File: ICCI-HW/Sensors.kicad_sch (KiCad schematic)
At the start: 25 parts, among them U301 DS18B20, U302 AS7341, U303 BH1750FVI-TR, U304 TCS34725FN, U305 TSL2561, U306 PCA9306GM,125

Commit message: hw: updates
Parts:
- U305: footprint ICCI-LIB:TLS2561 -> ICCI-LIB:TSL2561
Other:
- note added: "DS report no pull-up, Need testing."
- note removed: "DS report no pull-up, need testing."
- company: tollsimy -> Simone Tollardo
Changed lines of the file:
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@@
   (title_block
     (title "Sensors")
-    (date "2022-05-04")
+    (date "2022-07-14")
     (rev "BETA")
-    (company "tollsimy")
+    (company "Simone Tollardo")
   )
   (junction (at 78.105 134.62) (diameter 0) (color 0 0 0 0)
@@
     (effects (font (size 1.27 1.27)) (justify left bottom))
   )
-  (text "DS report\nno pull-up, \nneed testing." (at 69.215 118.11 0)
+  (text "DS report\nno pull-up, \nNeed testing." (at 69.215 118.11 0)
     (effects (font (size 1.27 1.27)) (justify left bottom))
   )
@@
     (effects (font (size 1.27 1.27)) (justify left bottom))
   )
-  (text "SENSORS" (at 62.865 19.685 180)
+  (text "SENSORS" (at 62.865 20.955 180)
     (effects (font (size 3 3) (thickness 0.6) bold) (justify right bottom))
   )
@@
     (property "Reference" "U305" (id 0) (at 63.5 85.725 0))
     (property "Value" "TSL2561" (id 1) (at 52.705 83.185 0))
-    (property "Footprint" "ICCI-LIB:TLS2561" (id 2) (at 52.705 94.615 0)
-      (effects (font (size 1.27 1.27)) (justify left bottom) hide)
-    )
+    (property "Footprint" "ICCI-LIB:TSL2561" (id 2) (at 52.705 94.615 0)
+      (effects (font (size 1.27 1.27)) (justify left bottom) hide)
+    )

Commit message: start layout
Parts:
- U301: footprint Package_TO_SOT_THT:TO-92_Inline -> ICCI-LIB:DS18B20 Hor.
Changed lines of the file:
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@@
       (effects (font (size 1.27 1.27)) (justify right))
     )
-    (property "Footprint" "Package_TO_SOT_THT:TO-92_Inline" (id 2) (at 21.59 175.895 0)
+    (property "Footprint" "ICCI-LIB:DS18B20 Hor." (id 2) (at 21.59 175.895 0)
       (effects (font (size 1.27 1.27)) hide)
     )

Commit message: layout updates
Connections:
- net ADDR: now reaches R302.1, U303.2 (ADDR)
- net DVI: now reaches C311.1, R303.2, U303.5 (DVI)
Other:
- moved on the sheet: R302
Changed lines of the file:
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@@
     (stroke (width 0) (type default) (color 0 0 0 0))
   )
-  (wire (pts (xy 62.865 70.485) (xy 64.135 70.485))
+  (wire (pts (xy 62.865 70.485) (xy 68.58 70.485))
     (stroke (width 0) (type default) (color 0 0 0 0))
   )
@@
     (effects (font (size 1.27 1.27)) (justify left bottom))
   )
+  (label "DVI" (at 64.77 51.435 0)
+    (effects (font (size 1.27 1.27)) (justify left bottom))
+  )
   (label "SDA0" (at 63.5 37.465 0)
     (effects (font (size 1.27 1.27)) (justify left bottom))
@@
     (effects (font (size 1.27 1.27)) (justify left bottom))
   )
+  (label "ADDR" (at 63.5 70.485 0)
+    (effects (font (size 1.27 1.27)) (justify left bottom))
+  )
   (hierarchical_label "SDA0" (shape bidirectional) (at 137.795 77.47 0)
     (effects (font (size 1.27 1.27)) (justify left))
@@
     (pin "2")
   )
-  (symbol (lib_id "Device:R") (at 64.135 74.295 0) (unit 1)
-    (in_bom yes) (on_board yes)
-    (property "Reference" "R302" (id 0) (at 65.405 73.025 0)
-      (effects (font (size 1.27 1.27)) (justify left))
-    )
-    (property "Value" "1k" (id 1) (at 65.405 75.565 0)
-      (effects (font (size 1.27 1.27)) (justify left))
-    )
-    (property "Footprint" "Resistor_SMD:R_0603_1608Metric" (id 2) (at 62.357 74.295 90)
-      (effects (font (size 1.27 1.27)) hide)
-    )
-    (property "Datasheet" "~" (id 3) (at 64.135 74.295 0)
+  (symbol (lib_id "Device:R") (at 68.58 74.295 0) (unit 1)
+    (in_bom yes) (on_board yes)
+    (property "Reference" "R302" (id 0) (at 69.85 73.025 0)
+      (effects (font (size 1.27 1.27)) (justify left))
+    )
+    (property "Value" "1k" (id 1) (at 69.85 75.565 0)
+      (effects (font (size 1.27 1.27)) (justify left))
+    )
+    (property "Footprint" "Resistor_SMD:R_0603_1608Metric" (id 2) (at 66.802 74.295 90)
+      (effects (font (size 1.27 1.27)) hide)
+    )
+    (property "Datasheet" "~" (id 3) (at 68.58 74.295 0)
       (effects (font (size 1.27 1.27)) hide)
     )
@@
     (pin "1")
   )
-  (symbol (lib_id "power:GND") (at 64.135 78.105 0) (unit 1)
-    (in_bom yes) (on_board yes)
-    (property "Reference" "#PWR0331" (id 0) (at 64.135 84.455 0)
-      (effects (font (size 1.27 1.27)) hide)
-    )
-    (property "Value" "GND" (id 1) (at 64.135 81.915 0))
-    (property "Footprint" "" (id 2) (at 64.135 78.105 0)
-      (effects (font (size 1.27 1.27)) hide)
-    )
-    (property "Datasheet" "" (id 3) (at 64.135 78.105 0)
-      (effects (font (size 1.27 1.27)) hide)
-    )
+  (symbol (lib_id "power:GND") (at 68.58 78.105 0) (unit 1)
+    (in_bom yes) (on_board yes)
+    (property "Reference" "#PWR0331" (id 0) (at 68.58 84.455 0)
+      (effects (font (size 1.27 1.27)) hide)
+    )
+    (property "Value" "GND" (id 1) (at 68.58 81.915 0))
+    (property "Footprint" "" (id 2) (at 68.58 78.105 0)
+      (effects (font (size 1.27 1.27)) hide)
+    )
+    (property "Datasheet" "" (id 3) (at 68.58 78.105 0)
+      (effects (font (size 1.27 1.27)) hide)
+    )

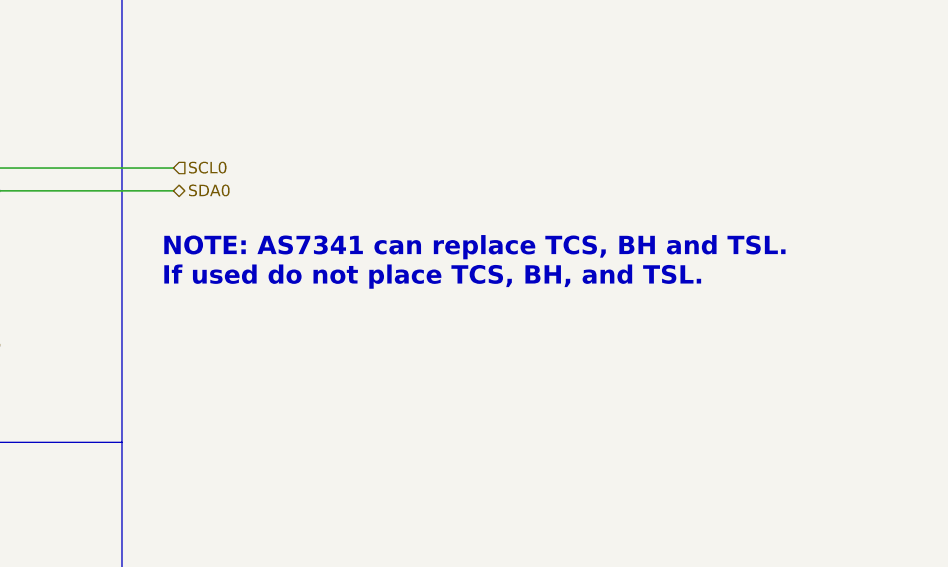
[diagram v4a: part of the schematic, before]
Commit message: hw: fix missing contact from SYS to SYSA on MAX77960
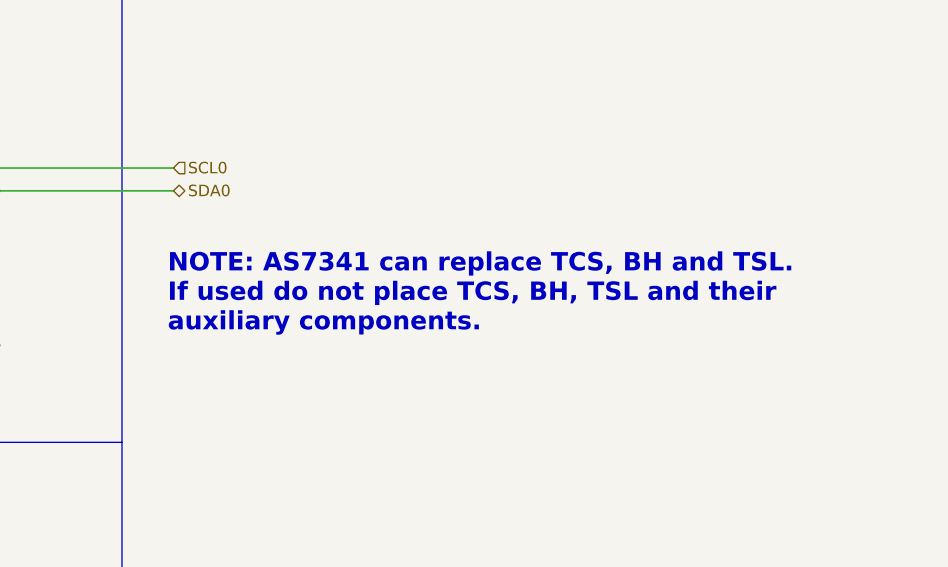
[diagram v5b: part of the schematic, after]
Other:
- note added: "NOTE: AS7341 can replace TCS, BH and TSL. If used do not place TCS, BH, TSL and their auxiliary components."
- note removed: "NOTE: AS7341 can replace TCS, BH and TSL. If used do not place TCS, BH, and TSL."
